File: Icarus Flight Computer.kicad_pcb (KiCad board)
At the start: 4 copper layers, 50 x 95 mm, 90 parts, among them J1 Conn_01x04_Socket, J2 JST PH 2.0, J3 USB_C_Receptacle_USB2.0_14P, J4 JST PH 2.0, J5 U.FL, J6 Screw_Terminal_01x06, Q1 DMG2305UX, Q2 Si7232DN, SW1 SW_Push, U1 STM32F405RGT6, U10 NEO-M9N-00B, U11 E220-900T22S, U2 W25Q128JVP, U3 USBLC6-2SC6, U4 TPS3839G33DBZ, U5 TPS631000, U6 ICM-45686, U7 ADXL375, U8 LIS2MDL, U9 MS5607-02BA, Y1 16MHz

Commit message: Added Docs folder
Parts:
- moved R16 0.29 mm to (156.6, 133.7)
- moved R18 0.29 mm to (156.2, 132.2)
- moved R20 0.29 mm to (157.9, 133.7)
- moved R22 0.29 mm to (158.4, 132.2)
- renumbered SW1 to BOOT
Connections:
- J2 pad 1: SERVO1_PWM -> GND
- J2 pad 2: SERVO2_PWM -> SERVO1_PWM
- J2 pad 3: SERVO3_PWM -> SERVO2_PWM
- J2 pad 4: SERVO4_PWM -> SERVO3_PWM
- J2 pad 5: GND -> SERVO4_PWM
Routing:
- net PYRO_VBAT: track 24.3 -> 28.7 mm
- net SERVO3_PWM: track 20.1 -> 23.8 mm
- net SERVO1_PWM: track 18.0 -> 21.5 mm
- net SERVO4_PWM: track 21.3 -> 24.3 mm
- net SERVO2_PWM: track 19.7 -> 22.6 mm
- net GND: track 68.9 -> 71.2 mm, vias 80 -> 83
- net +3.3V: track 40.3 -> 38.0 mm, vias 38 -> 36
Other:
- board text added: "+"
- board text added: "-"
- board text added: "1"
- board text added: "2"
- board text added: "3"
- board text added: "4"
- board text added: "Battery"
- board text added: "GND"
- board text added: "Pyro A"
- board text added: "Pyro B"
- board text added: "SERVOS"
- board text added: "X"
- board text added: "Y"
- board text added: "Z"

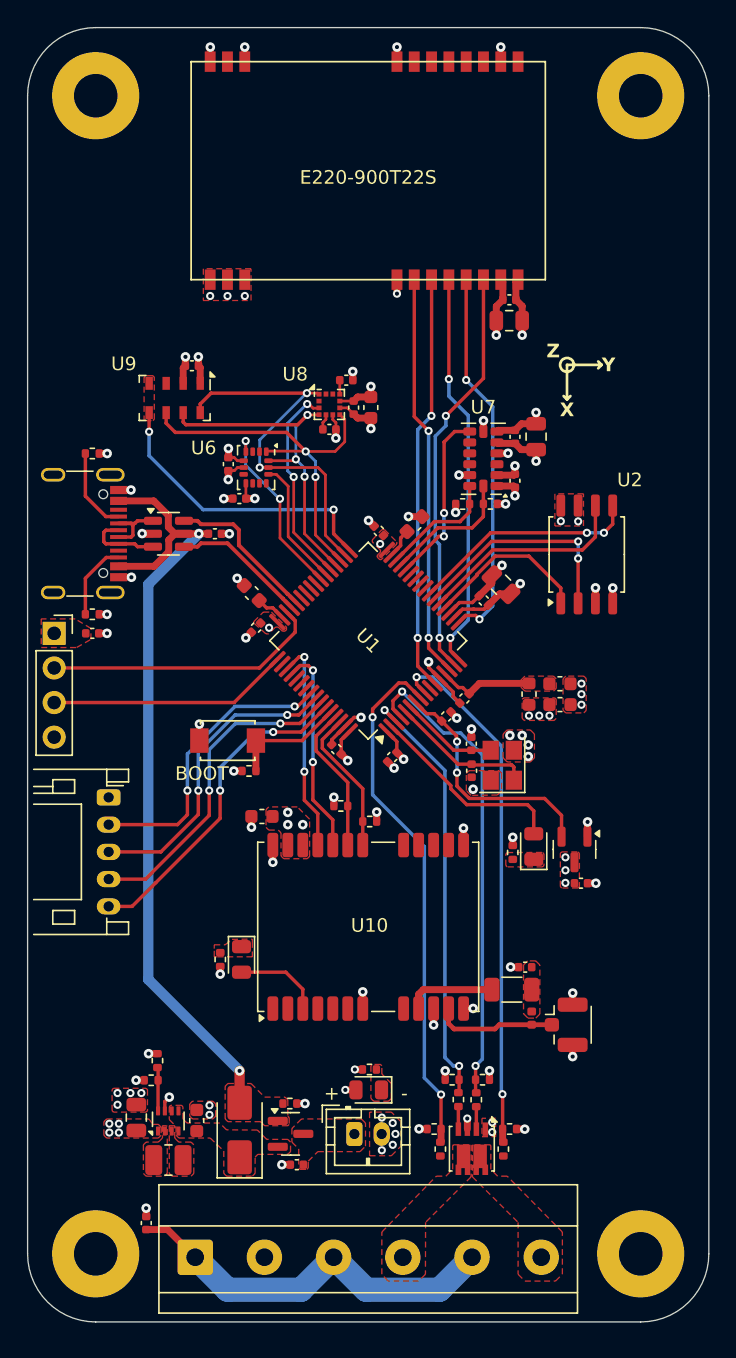
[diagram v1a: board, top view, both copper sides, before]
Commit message: Made board smaller
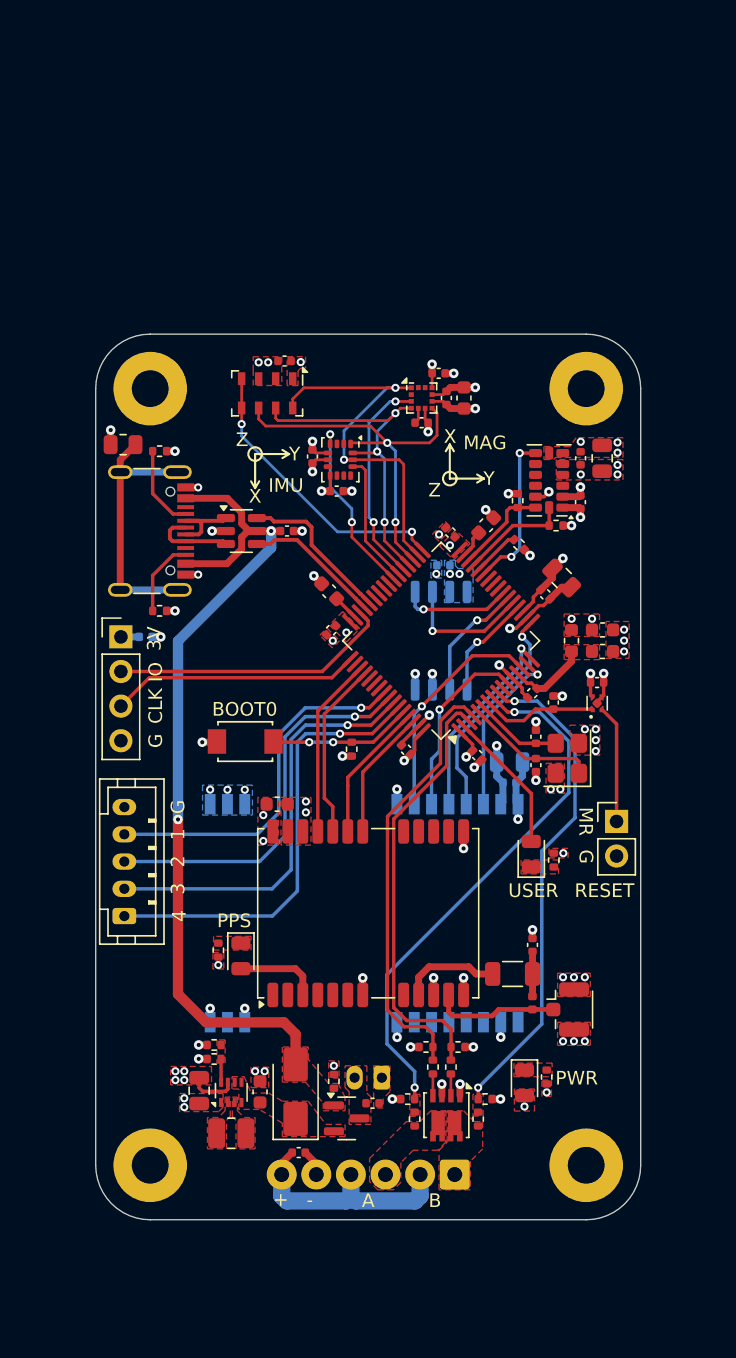
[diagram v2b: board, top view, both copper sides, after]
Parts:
- removed BOOT: SW_Push, Button_Switch_SMD:SW_TS-1088-AR02016
- added C36: 100n, Capacitor_SMD:C_0402_1005Metric, F.Cu at (144.9, 137.6)
- added G***: LOGO, Daedalus_Industries:Icarus_Flight_Computer, B.Cu at (165.5, 110.7)
- added J7: Screw_Terminal_01x06, TerminalBlock_Phoenix:TerminalBlock_Phoenix_MPT-0,5-6-2.54_1x06_P2.54mm_Horizontal, B.Cu at (156.3, 139.2)
- added SW1: SW_Push, Button_Switch_SMD:SW_TS-1088-AR02016, F.Cu at (141.0, 107.4)
- C11: value 10p -> 100n; moved to B.Cu
- C13: value 100n -> 10p
- C16, C35, J4, U11: moved to B.Cu
- C19: value 47u -> 100n; footprint Capacitor_SMD:C_0805_2012Metric -> Capacitor_SMD:C_0402_1005Metric
- C20: value 10u -> 47u; footprint Capacitor_SMD:C_0603_1608Metric -> Capacitor_SMD:C_0805_2012Metric
- C21: value 100n -> 10u; footprint Capacitor_SMD:C_0402_1005Metric -> Capacitor_SMD:C_0603_1608Metric
- C23, C33: value 10u -> 100n; footprint Capacitor_SMD:C_0805_2012Metric -> Capacitor_SMD:C_0402_1005Metric
- C24: value 100n -> 10u; footprint Capacitor_SMD:C_0402_1005Metric -> Capacitor_SMD:C_0805_2012Metric
- C27: value 1u -> 100n; footprint Capacitor_SMD:C_0603_1608Metric -> Capacitor_SMD:C_0402_1005Metric
- C28, C32: value 100n -> 1u; footprint Capacitor_SMD:C_0402_1005Metric -> Capacitor_SMD:C_0603_1608Metric
- C30: value 220n -> 100n
- C31: value 1u -> 220n; footprint Capacitor_SMD:C_0603_1608Metric -> Capacitor_SMD:C_0402_1005Metric
- C34: value 100n -> 10u; footprint Capacitor_SMD:C_0402_1005Metric -> Capacitor_SMD:C_0805_2012Metric; moved to B.Cu
- H1, H2, H3, H4: footprint MountingHole:MountingHole_3.2mm_M3_Pad -> MountingHole:MountingHole_2.7mm_M2.5_Pad
- J1: value Conn_01x04_Socket -> Conn_01x04_Pin; footprint Connector_PinSocket_2.54mm:PinSocket_1x04_P2.54mm_Vertical -> Connector_PinHeader_2.54mm:PinHeader_1x04_P2.54mm_Vertical
- J2: footprint Connector_JST:JST_PH_S5B-PH-K_1x05_P2.00mm_Horizontal -> Connector_JST:JST_PH_B5B-PH-K_1x05_P2.00mm_Vertical
- J5: value U.FL -> Conn_01x02_Pin; footprint Connector_Coaxial:U.FL_Hirose_U.FL-R-SMT-1_Vertical -> Connector_PinHeader_2.54mm:PinHeader_1x02_P2.54mm_Vertical
- J6: value Screw_Terminal_01x06 -> U.FL; footprint TerminalBlock_Phoenix:TerminalBlock_Phoenix_MKDS-1,5-6-5.08_1x06_P5.08mm_Horizontal -> Connector_Coaxial:U.FL_Hirose_U.FL-R-SMT-1_Vertical
- R2: value 1k -> 10k
- R3: value 2k -> 1k
- R6: value 2k -> 5k1
- R8: value 5k1 -> 0R; footprint Resistor_SMD:R_0402_1005Metric -> Resistor_SMD:R_0805_2012Metric
- U2: value W25Q128JVP -> W25Q128JVSIQ; moved to B.Cu
- U4: value TPS3839G33DBZ -> TPS3831G33DQNR; footprint Package_TO_SOT_SMD:SOT-23 -> Package_SON:Texas_X2SON-4_1x1mm_P0.65mm
- moved U11 70.5 mm to (161.0, 128.0)
- moved C17 46.5 mm to (144.0, 91.9), turned to 0 degrees
- moved C21 46.1 mm to (142.1, 133.1), turned to 90 degrees
- moved C33 45.9 mm to (162.1, 122.3), turned to 90 degrees
- moved C35 41.9 mm to (160.4, 110.4), turned to 0 degrees
- moved C34 33.9 mm to (160.4, 108.9)
- moved C13 33.4 mm to (162.3, 107.0), turned to 90 degrees
- moved J6 32.8 mm to (164.6, 127.1)
- moved C31 31.2 mm to (153.9, 84.0), turned to 0 degrees
- moved C26 30.2 mm to (165.6, 89.8), turned to 90 degrees
- moved R3 26.6 mm to (163.6, 116.1), turned to 90 degrees
- moved R5 25.9 mm to (161.0, 89.7), turned to -90 degrees
- moved C11 25.9 mm to (133.7, 99.7), turned to 0 degrees
- moved R2 22.6 mm to (161.1, 92.9), turned to -45 degrees
- moved H3 21.9 mm to (166.0, 81.5)
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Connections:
- C11 pad 1: /MCU/HSE_IN -> +3.3V
- C12 pad 1: /MCU/HSE_OUT -> /MCU/HSE_IN
- C13 pad 1: +3.3V -> /MCU/HSE_OUT
- C16 pad 1: VBUS -> +3.3V
- C17 pad 1: VBAT -> VBUS
- C19 pad 1: +3.3V -> VBAT
- C20 pad 1: /Power/VIN -> +3.3V
- C21 pad 1: +3.3V -> /Power/VIN
- C30 pad 1: /Sensors/C1 -> +3.3V
- C31 pad 1: +3.3V -> /Sensors/C1
- C32 pad 1: /GPS/BIAS_T -> +3.3V
- C33 pad 1: +3.3V -> /GPS/BIAS_T
- C35 pad 1: PYRO_VBAT -> +3.3V
- J2 pad 1: GND -> SERVO4_PWM
- J2 pad 2: SERVO1_PWM -> SERVO3_PWM
- J2 pad 4: SERVO3_PWM -> SERVO1_PWM
- J2 pad 5: SERVO4_PWM -> GND
- J3 pad S1: unconnected-(J3-SHIELD-PadS1)_3 -> /USB/SHIELD
- J4 pad 1: VBAT -> GND
- J4 pad 2: GND -> VBAT
- J5 pad 1: /GPS/GPS_ANT -> /Power/~{MR}
- J6 pad 1: PYRO_VBAT -> /GPS/GPS_ANT
- R2 pad 1: /MCU/USER_LED_K -> /MCU/BOOT1
- R3 pad 1: +3.3V -> /MCU/USER_LED_K
- R3 pad 2: ACC_I2C_SCL -> GND
- R4 pad 2: ACC_I2C_SDA -> ACC_I2C_SCL
- R5 pad 2: GPS_I2C_SCL -> ACC_I2C_SDA
- R6 pad 1: +3.3V -> /USB/CC2
- R6 pad 2: GPS_I2C_SDA -> GND
- R7 pad 1: /USB/CC2 -> /USB/CC1
- R8 pad 1: /USB/CC1 -> /USB/SHIELD
- U1 pad 27: unconnected-(U1-PB1-Pad27) -> ACC_INT
- U1 pad 28: ACC_INT -> /MCU/BOOT1
- U1 pad 3: PYRO_A_FIRE -> PYRO_B_FIRE
- U1 pad 4: PYRO_B_FIRE -> PYRO_A_FIRE
- U4 pad 1: GND -> ~{RESET}
- U4 pad 2: ~{RESET} -> /Power/~{MR}
- U4 pad 3: +3.3V -> GND
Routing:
- net /USB/SHIELD: track 0.00 -> 19.5 mm
- net RF_AUX: track 30.3 -> 12.6 mm, vias 2 -> 1
- net RF_M1: track 30.6 -> 13.6 mm, vias 2 -> 1
- net RF_UART_RX: track 29.4 -> 14.7 mm, vias 2 -> 1
- net RF_M0: track 29.6 -> 16.7 mm, vias 2 -> 1
- net RF_UART_TX: track 28.0 -> 16.4 mm, vias 2 -> 1
- net PYRO_VBAT: track 28.7 -> 17.4 mm
- net ~{RESET}: track 17.8 -> 8.51 mm, vias 2 -> 0
- net FLASH_SPI_MOSI: track 16.9 -> 8.11 mm, vias 2 -> 1
- net /Power/~{MR}: track 0.00 -> 8.62 mm
- net SERVO4_PWM: track 24.3 -> 32.9 mm, vias 2 -> 1
- net FLASH_SPI_MISO: track 16.8 -> 8.90 mm, vias 2 -> 1
- net SERVO3_PWM: track 23.8 -> 31.0 mm, vias 2 -> 1
- net FLASH_SPI_SCK: track 15.7 -> 9.62 mm, vias 0 -> 1
- net GND: track 71.2 -> 65.1 mm, vias 83 -> 84
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- added copper zone on B.Cu, net +3.3V
- added copper zone on F.Cu, net /Power/FB
- added copper zone on B.Cu, net GND
- added copper zone on F.Cu, net PYRO_A_SENSE
- added copper zone on F.Cu, net PYRO_B_SENSE
- removed copper zone on F.Cu, net /GPS/BIAS_T
- removed copper zone on F.Cu, net BAR_CS
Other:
- board size 50 x 95 mm -> 40 x 65 mm
- board text added: "3V"
- board text added: "A"
- board text added: "B"
- board text added: "BOOT0"
- board text added: "CLK"
- board text added: "Designer: Mattia Gregnanin"
- board text added: "G"
- board text added: "IMU"
- board text added: "IO"
- board text added: "MAG"
- board text added: "MR"
- board text added: "PPS"
- board text added: "PWR"
- board text added: "RESET"
- board text added: "Revision: V1.0"
- board text added: "USER"
- board text removed: "Battery"
- board text removed: "GND"
- board text removed: "Icarus Flight Computer V1.0"
- board text removed: "Pyro A"
- board text removed: "Pyro B"
- board text removed: "SERVOS"

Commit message: V1.0
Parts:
- removed the C11 at (133.7, 99.7)
- removed the C28 at (157.0, 82.2)
- removed the J2 at (132.1, 120.2)
- added C26: 100n, Capacitor_SMD:C_0402_1005Metric, F.Cu at (151.7, 82.5)
- added C27: 100n, Capacitor_SMD:C_0402_1005Metric, F.Cu at (153.4, 87.2)
- added C29: 10u, Capacitor_SMD:C_0805_2012Metric, F.Cu at (141.2, 79.8)
- added D5: PESD3V3L1BA, Diode_SMD:D_SOD-323, B.Cu at (133.0, 121.2)
- added D6: PESD3V3L1BA, Diode_SMD:D_SOD-323, B.Cu at (134.1, 118.2)
- added D7: PESD3V3L1BA, Diode_SMD:D_SOD-323, B.Cu at (134.1, 116.2)
- added D8: PESD3V3L1BA, Diode_SMD:D_SOD-323, B.Cu at (133.0, 113.1)
- added J7: JST PH 2.0, Connector_JST:JST_PH_B5B-PH-K_1x05_P2.00mm_Vertical, F.Cu at (131.0, 120.2)
- added R1: 22R, Resistor_SMD:R_0402_1005Metric, F.Cu at (145.5, 102.3)
- added R2: 22R, Resistor_SMD:R_0402_1005Metric, F.Cu at (145.5, 103.3)
- added R27: 47R, Resistor_SMD:R_0402_1005Metric, B.Cu at (145.0, 108.5)
- added R28: 47R, Resistor_SMD:R_0402_1005Metric, F.Cu at (139.0, 118.2)
- added R29: 47R, Resistor_SMD:R_0402_1005Metric, F.Cu at (139.0, 116.2)
- added R30: 47R, Resistor_SMD:R_0402_1005Metric, B.Cu at (146.7, 104.9)
- added R8: 2k, Resistor_SMD:R_0402_1005Metric, F.Cu at (139.9, 85.5)
- added R9: 2k, Resistor_SMD:R_0402_1005Metric, F.Cu at (142.4, 85.5)
- H1, H2, H3, H4: footprint MountingHole:MountingHole_2.7mm_M2.5_Pad -> MountingHole:MountingHole_2.7mm_M2.5_Pad_Via
- J5: renamed from J6; value U.FL -> SMA; footprint Connector_Coaxial:U.FL_Hirose_U.FL-R-SMT-1_Vertical -> Connector_Coaxial:SMA_Amphenol_132134_Vertical
- R16: renamed from R12; value 10k -> 100k
- U11: footprint E220:PE220-400T22S -> My_RF_Module:E220-xxxT22S
- U9: footprint Package_LGA:LGA-8_3x5mm_P1.25mm -> My_Sensor:MS5607-02BA03
- moved C30 16.4 mm to (139.4, 81.9), turned to 90 degrees
- moved C28 15.2 mm to (158.4, 84.0), turned to 90 degrees
- moved C31 14.0 mm to (141.2, 81.4)
- moved U11 13.8 mm to (149.7, 120.0), turned to 90 degrees
- moved U9 13.5 mm to (156.0, 82.8), turned to 180 degrees
- moved U8 12.8 mm to (141.2, 83.2), turned to 90 degrees
- moved C32 11.0 mm to (143.0, 83.2), turned to 90 degrees
- moved G*** 7.74 mm to (166.8, 103.1)
- moved C37 4.56 mm to (140.6, 139.2), turned to 180 degrees
- moved R17 4.47 mm to (159.4, 120.1), turned to -90 degrees
- moved L2 3.04 mm to (159.5, 125.0)
- moved D2 2.77 mm to (161.8, 135.2)
- moved R14 2.77 mm to (163.4, 134.8)
- moved J5 2.72 mm to (166.8, 125.5)
- moved G*** 2.34 mm to (144.3, 92.8)
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- renumbered C12 to C11, C13 to C12, C14 to C13, C15 to C14, C16 to C15, C17 to C16, C18 to C17, C19 to C18, C20 to C19, C21 to C20, C22 to C21, C23 to C22, C24 to C23, C25 to C24, C26 to C25, C27 to C28, C29 to C30, C30 to C31, C31 to C32, C32 to C33, C33 to C34, C34 to C35, C35 to C36, C36 to C37, J3 to J2, J4 to J3, J5 to J4, J7 to J6, R6 to R10, R7 to R11, R8 to R12, R9 to R13, R10 to R14, R11 to R15, R13 to R17, R14 to R18, R15 to R19, R16 to R20, R17 to R21, R18 to R22, R19 to R23, R20 to R24, R21 to R25, R22 to R26, R1 to R3, R2 to R4, R3 to R5, R4 to R6, R5 to R7
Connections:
- net /MCU/BOOT0 renamed BOOT0
- net /MCU/BOOT1 renamed BOOT1
- net /MCU/HSE_IN renamed HSE_IN
- net /MCU/HSE_OUT renamed HSE_OUT
- J1 pad 2: SWDIO -> /MCU/SW_DIO_HEADER
- J1 pad 3: SWCLK -> /MCU/SW_CLK_HEADER
- U1 pad 37: MAG_CS -> IMU_CS
- U1 pad 38: IMU_CS -> IMU_INT
- U1 pad 39: IMU_INT -> unconnected-(U1-PC8-Pad39)
- U1 pad 40: unconnected-(U1-PC9-Pad40) -> MAG_I2C_SDA
- U1 pad 41: unconnected-(U1-PA8-Pad41) -> MAG_I2C_SCL
- U1 pad 46: SWDIO -> SW_DIO
- U1 pad 49: SWCLK -> SW_CLK
- U8 pad 1: SPI2_SCK -> MAG_I2C_SCL
- U8 pad 3: MAG_CS -> +3.3V
- U8 pad 4: SPI2_MOSI -> MAG_I2C_SDA
- U8 pad 7: SPI2_MISO -> unconnected-(U8-DRDY-Pad7)
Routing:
- net SERVO4_PWM: track 32.9 -> 8.96 mm
- net /Servo/SERVO4_PWM_HEADER: track 0.00 -> 23.2 mm
- net SERVO1_PWM: track 26.7 -> 4.40 mm
- net /Servo/SERVO1_PWM_HEADER: track 0.00 -> 22.3 mm
- net SWDIO: track 20.7 -> 0.00 mm
- net SWCLK: track 18.3 -> 0.00 mm
- net MAG_I2C_SCL: track 0.00 -> 16.7 mm
- net MAG_I2C_SDA: track 0.00 -> 15.9 mm
- net MAG_CS: track 15.6 -> 0.00 mm, vias 2 -> 0
- net /MCU/SW_CLK_HEADER: track 0.00 -> 14.6 mm
- net /MCU/SW_DIO_HEADER: track 0.00 -> 14.0 mm
- net SPI2_SCK: track 28.5 -> 14.7 mm
- net GND: track 65.1 -> 53.1 mm, vias 84 -> 129
- net SPI2_MOSI: track 25.8 -> 16.0 mm, vias 3 -> 0
- net +3.3V: track 32.8 -> 41.3 mm, vias 30 -> 34
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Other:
- board size 40 x 65 mm -> 42 x 65 mm
- board text added: "ANT"
- board text added: "BAT"
- board text removed: "RESET"
